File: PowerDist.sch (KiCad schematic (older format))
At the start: 12 parts, among them U4 RI3-1205S, U5 NCP1117-3.3_SOT223

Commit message: Fixing merge issues
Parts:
- U4: symbol utsvt-power-regulators:RI3-1205S -> Controls-LightingPCB-rescue:RI3-1205S-utsvt-power-regulators
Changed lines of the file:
@@
 	8750 3200 8550 3200
 $Comp
-L utsvt-power-regulators:RI3-1205S U4
+L Controls-LightingPCB-rescue:RI3-1205S-utsvt-power-regulators U4
 U 1 1 5C38C4FE
 P 4500 3200

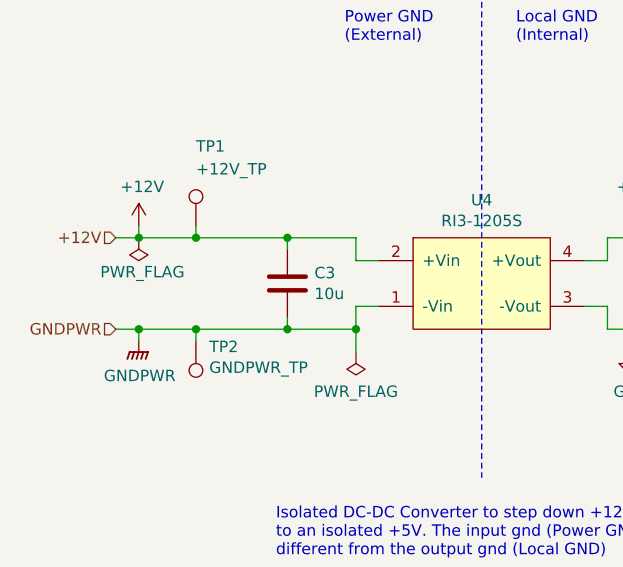
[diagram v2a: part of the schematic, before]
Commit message: Added resistor and diode
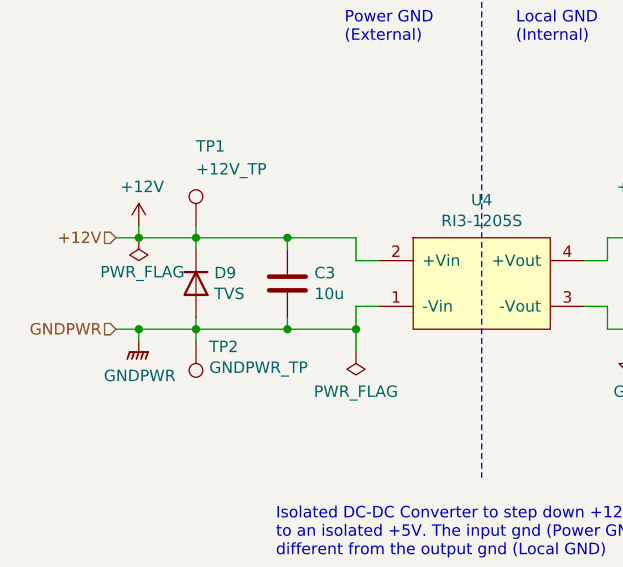
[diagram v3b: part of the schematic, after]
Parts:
- added D9: TVS, Diode_SMD:D_SOD-323, symbol Simulation_SPICE:DIODE
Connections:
- net +12V: now also D9.2 (K)
- net GNDPWR: now also D9.1 (A)
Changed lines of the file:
@@
 Wire Wire Line
 	2900 3600 3000 3600
+$Comp
+L Simulation_SPICE:DIODE D9
+U 1 1 615A7A80
+P 3250 3400
+F 0 "D9" V 3296 3320 50  0000 R CNN
+F 1 "TVS" V 3205 3320 50  0000 R CNN
+F 2 "Diode_SMD:D_SOD-323" H 3250 3400 50  0001 C CNN
+F 3 "~" H 3250 3400 50  0001 C CNN
+F 4 "Y" H 3250 3400 50  0001 L CNN "Spice_Netlist_Enabled"
+F 5 "D" H 3250 3400 50  0001 L CNN "Spice_Primitive"
+	1    3250 3400
+	0    -1   -1   0
+$EndComp
+Wire Wire Line
+	3250 3250 3250 3200
+Wire Wire Line
+	3250 3550 3250 3600
 $EndSCHEMATC

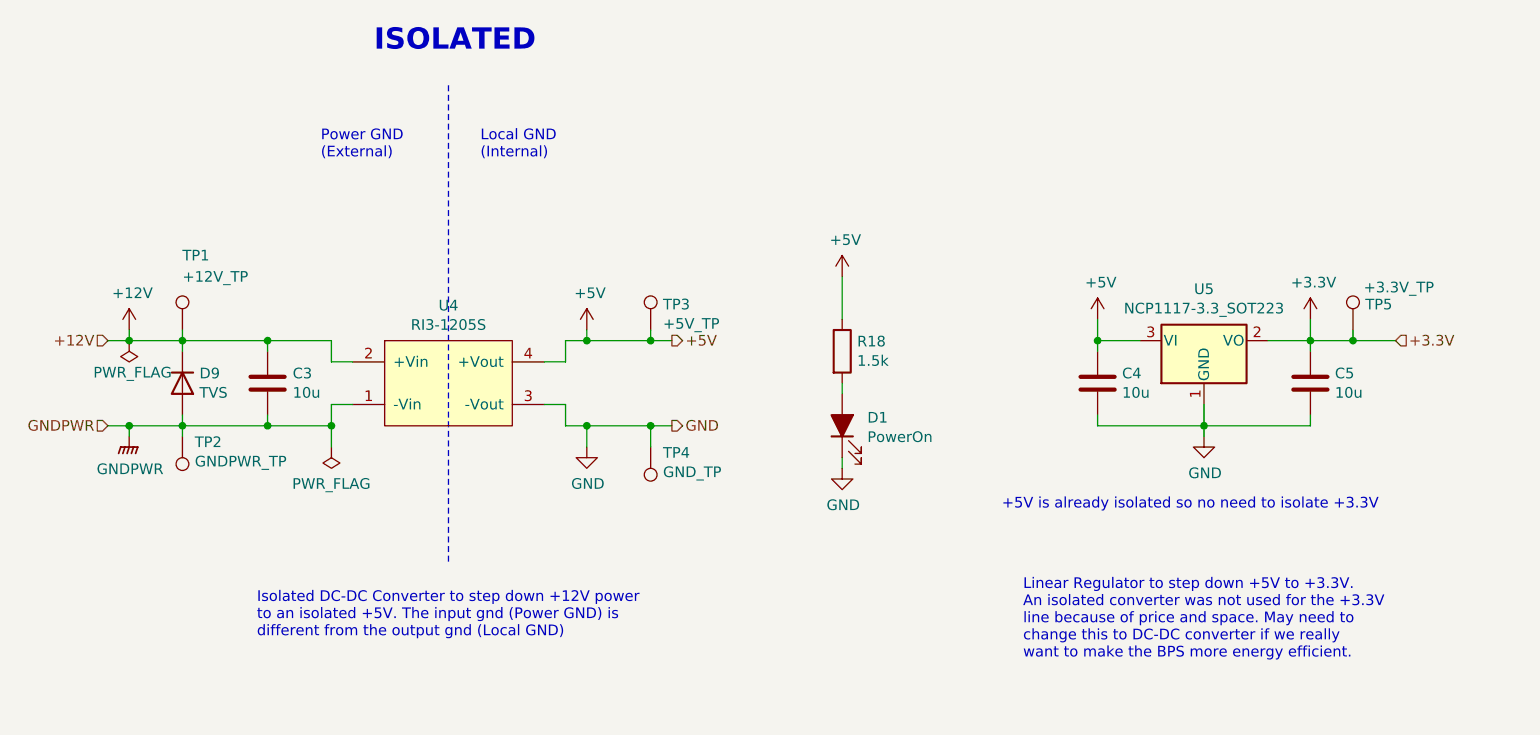
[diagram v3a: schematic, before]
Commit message: isoSPI -> SPI change
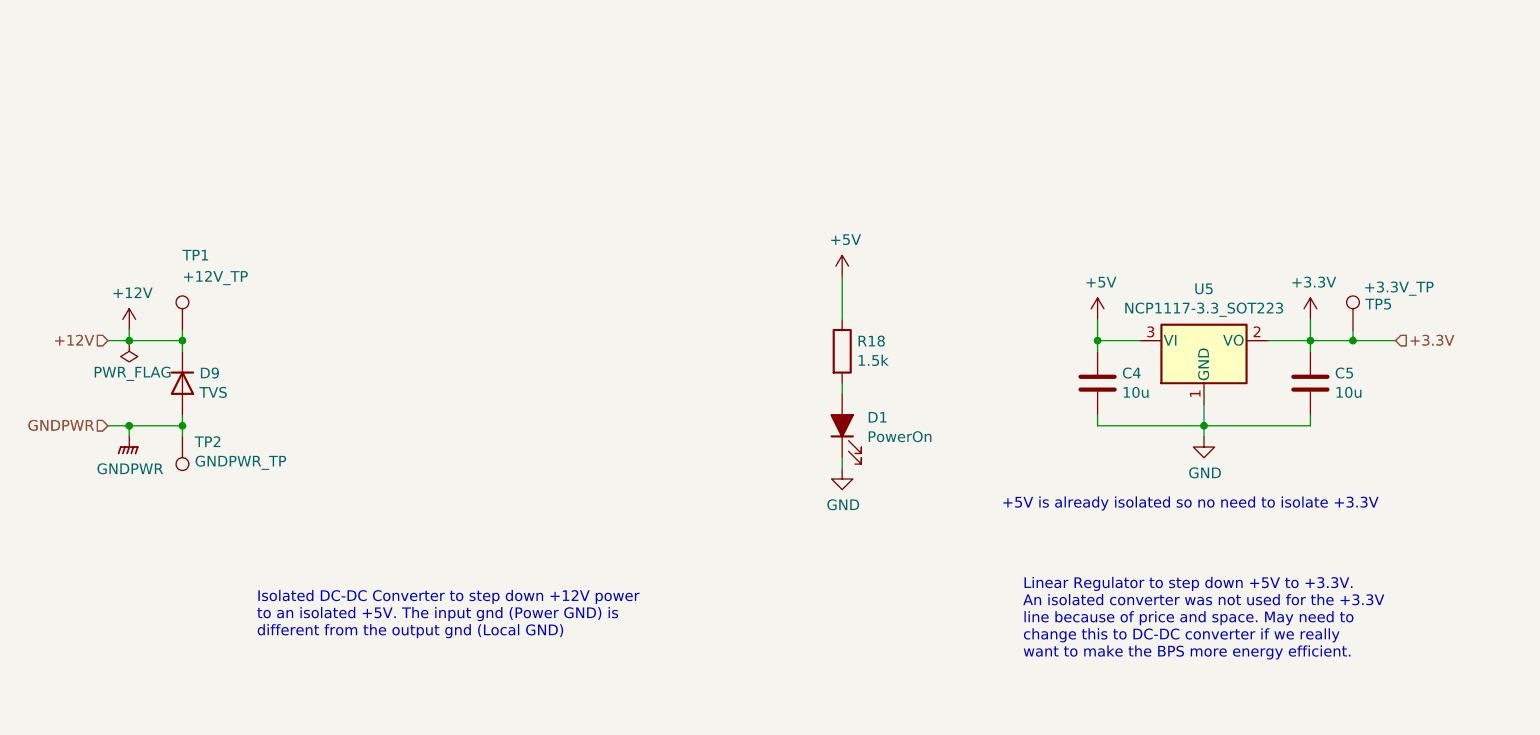
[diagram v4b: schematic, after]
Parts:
- removed C3: 10u, UTSVT_Passive:C_2220_5750Metric, symbol Device:C
- removed TP3: +5V_TP, TestPoint:TestPoint_Pad_1.5x1.5mm, symbol Connector:TestPoint
- removed TP4: GND_TP, TestPoint:TestPoint_Pad_1.5x1.5mm, symbol Connector:TestPoint
- removed U4: RI3-1205S, UTSVT_ICs:RI3_DC_Converter, symbol Controls-LightingPCB-rescue:RI3-1205S-utsvt-power-regulators
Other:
- note removed: "ISOLATED"
- note removed: "Local GND\n(Internal)"
- note removed: "Power GND\n(External)"
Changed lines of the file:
@@
 Wire Wire Line
 	3000 3600 3000 3650
-$Comp
-L Device:C C3
-U 1 1 5C35F7E4
-P 3650 3400
-F 0 "C3" H 3768 3446 50  0000 L CNN
-F 1 "10u" H 3768 3355 50  0000 L CNN
-F 2 "UTSVT_Passive:C_2220_5750Metric" H 3688 3250 50  0001 C CNN
-F 3 "~" H 3650 3400 50  0001 C CNN
-	1    3650 3400
-	1    0    0    -1
-$EndComp
 Wire Wire Line
 	3000 3600 3250 3600
@@
 	3000 3200 3250 3200
 Connection ~ 3000 3200
-Wire Wire Line
-	3650 3250 3650 3200
 Connection ~ 3250 3200
-Wire Wire Line
-	3650 3550 3650 3600
-Wire Wire Line
-	5150 3700 5150 3600
-Connection ~ 5150 3600
-Wire Wire Line
-	5450 3600 5150 3600
-Wire Wire Line
-	5150 3150 5150 3200
-Text HLabel 5550 3600 2    50   Output ~ 0
-GND
-Wire Wire Line
-	5550 3600 5450 3600
-Connection ~ 5450 3600
-Text HLabel 5550 3200 2    50   Output ~ 0
-+5V
-$Comp
-L power:+5V #PWR04
-U 1 1 5C376123
-P 5150 3150
-F 0 "#PWR04" H 5150 3000 50  0001 C CNN
-F 1 "+5V" H 5165 3323 50  0000 C CNN
-F 2 "" H 5150 3150 50  0001 C CNN
-F 3 "" H 5150 3150 50  0001 C CNN
-	1    5150 3150
-	1    0    0    -1
-$EndComp
 $Comp
 L Connector:TestPoint TP1
@@
 Wire Wire Line
 	3250 3150 3250 3200
-$Comp
-L Connector:TestPoint TP3
-U 1 1 5C37E6A3
-P 5450 3150
-F 0 "TP3" H 5508 3270 50  0000 L CNN
-F 1 "+5V_TP" H 5508 3179 50  0000 L CNN
-F 2 "TestPoint:TestPoint_Pad_1.5x1.5mm" H 5650 3150 50  0001 C CNN
-F 3 "~" H 5650 3150 50  0001 C CNN
-	1    5450 3150
-	1    0    0    -1
-$EndComp
-Wire Wire Line
-	5450 3150 5450 3200
-$Comp
-L Connector:TestPoint TP4
-U 1 1 5C37F6B1
-P 5450 3700
-F 0 "TP4" H 5392 3727 50  0000 R CNN
-F 1 "GND_TP" H 5392 3818 50  0000 R CNN
-F 2 "TestPoint:TestPoint_Pad_1.5x1.5mm" H 5650 3700 50  0001 C CNN
-F 3 "~" H 5650 3700 50  0001 C CNN
-	1    5450 3700
-	-1   0    0    1
-$EndComp
-Wire Wire Line
-	5450 3700 5450 3600
 $Comp
 L power:GND #PWR07
@@
 $EndComp
 $Comp
-L power:GND #PWR05
-U 1 1 5C3F3B1F
-P 5150 3700
-F 0 "#PWR05" H 5150 3450 50  0001 C CNN
-F 1 "GND" H 5155 3527 50  0000 C CNN
-F 2 "" H 5150 3700 50  0001 C CNN
-F 3 "" H 5150 3700 50  0001 C CNN
-	1    5150 3700
-	1    0    0    -1
-$EndComp
-$Comp
 L power:GNDPWR #PWR03
 U 1 1 5C3F7204
@@
 Wire Wire Line
 	8750 3200 8550 3200
-$Comp
-L Controls-LightingPCB-rescue:RI3-1205S-utsvt-power-regulators U4
-U 1 1 5C38C4FE
-P 4500 3200
-F 0 "U4" H 4500 3365 50  0000 C CNN
-F 1 "RI3-1205S" H 4500 3274 50  0000 C CNN
-F 2 "UTSVT_ICs:RI3_DC_Converter" H 4500 3200 50  0001 C CNN
-F 3 "" H 4500 3200 50  0001 C CNN
-	1    4500 3200
-	1    0    0    -1
-$EndComp
-Wire Wire Line
-	3950 3500 4050 3500
-Wire Wire Line
-	3950 3300 4050 3300
-Wire Wire Line
-	4950 3300 5050 3300
-Wire Wire Line
-	5050 3300 5050 3200
-Wire Wire Line
-	4950 3500 5050 3500
-Wire Wire Line
-	5050 3500 5050 3600
-Wire Wire Line
-	5050 3600 5150 3600
-Wire Wire Line
-	5050 3200 5150 3200
-Connection ~ 5150 3200
-Wire Wire Line
-	5150 3200 5450 3200
-Connection ~ 5450 3200
-Wire Wire Line
-	5450 3200 5550 3200
 $Comp
 L Connector:TestPoint TP2
@@
 +5V is already isolated so no need to isolate +3.3V
 $Comp
-L power:PWR_FLAG #FLG02
-U 1 1 5F1EAFA2
-P 3950 3700
-F 0 "#FLG02" H 3950 3775 50  0001 C CNN
-F 1 "PWR_FLAG" H 3950 3873 50  0000 C CNN
-F 2 "" H 3950 3700 50  0001 C CNN
-F 3 "~" H 3950 3700 50  0001 C CNN
-	1    3950 3700
-	-1   0    0    1
-$EndComp
-$Comp
 L power:PWR_FLAG #FLG01
 U 1 1 5F1F32D3
@@
 Wire Wire Line
 	2900 3200 3000 3200
-Text Notes 4150 1850 0    100  ~ 20
-ISOLATED
-Text Notes 4650 2350 0    50   ~ 0
-Local GND\n(Internal)
-Text Notes 3900 2350 0    50   ~ 0
-Power GND\n(External)
 Text Notes 7200 4700 0    50   ~ 0
 Linear Regulator to step down +5V to +3.3V.\nAn isolated converter was not used for the +3.3V\nline because of price and space. May need to\nchange this to DC-DC converter if we really\nwant to make the BPS more energy efficient.
-Wire Notes Line
-	4500 2000 4500 4250
 Text Notes 3600 4600 0    50   ~ 0
 Isolated DC-DC Converter to step down +12V power\nto an isolated +5V. The input gnd (Power GND) is\ndifferent from the output gnd (Local GND)
-Wire Wire Line
-	3250 3200 3650 3200
-Connection ~ 3650 3200
-Wire Wire Line
-	3650 3200 3950 3200
-Wire Wire Line
-	3250 3600 3650 3600
 Connection ~ 3250 3600
-Connection ~ 3650 3600
-Wire Wire Line
-	3650 3600 3950 3600
-Wire Wire Line
-	3950 3200 3950 3300
-Connection ~ 3950 3600
-Wire Wire Line
-	3950 3600 3950 3700
-Wire Wire Line
-	3950 3500 3950 3600
 Wire Wire Line
 	6350 2900 6350 3100

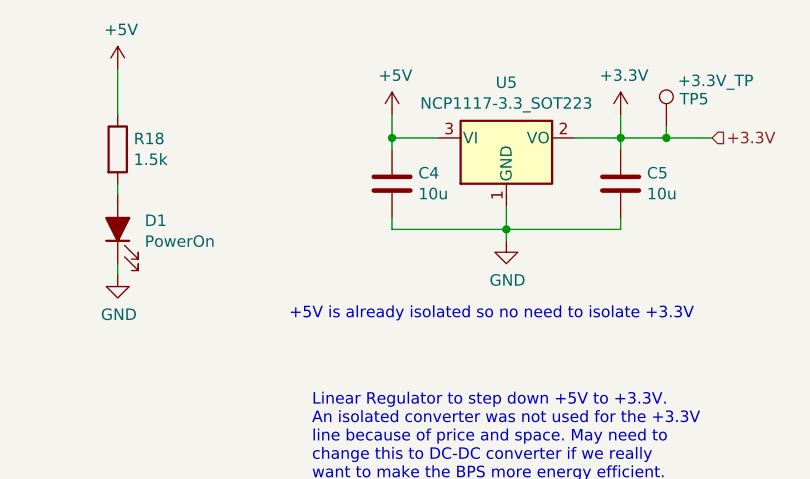
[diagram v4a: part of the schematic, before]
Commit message: isoSPI -> SPI 2
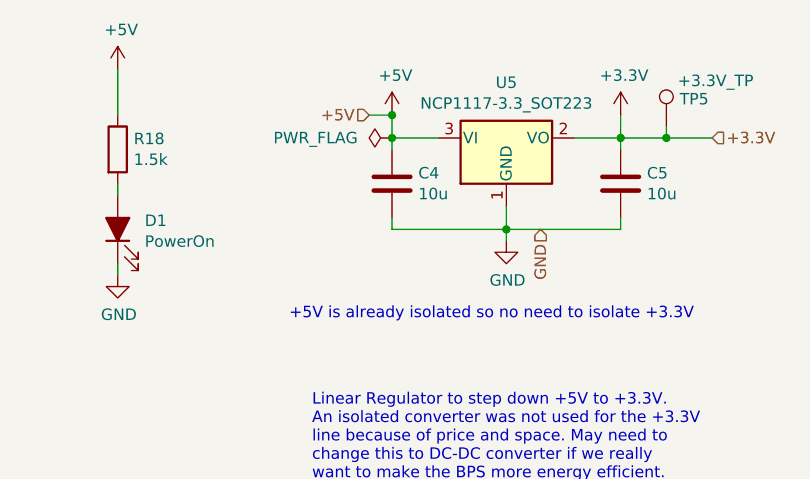
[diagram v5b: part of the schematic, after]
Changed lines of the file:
@@
 Wire Wire Line
 	3250 3550 3250 3600
+$Comp
+L power:PWR_FLAG #FLG0101
+U 1 1 61A11CC9
+P 7550 3200
+F 0 "#FLG0101" H 7550 3275 50  0001 C CNN
+F 1 "PWR_FLAG" V 7550 3350 50  0000 L CNN
+F 2 "" H 7550 3200 50  0001 C CNN
+F 3 "~" H 7550 3200 50  0001 C CNN
+	1    7550 3200
+	0    -1   -1   0
+$EndComp
+Wire Wire Line
+	7450 3100 7550 3100
+Connection ~ 7550 3100
+Text HLabel 7450 3100 0    50   Input ~ 0
++5V
+Text HLabel 8200 3600 3    50   Input ~ 0
+GND
 $EndSCHEMATC

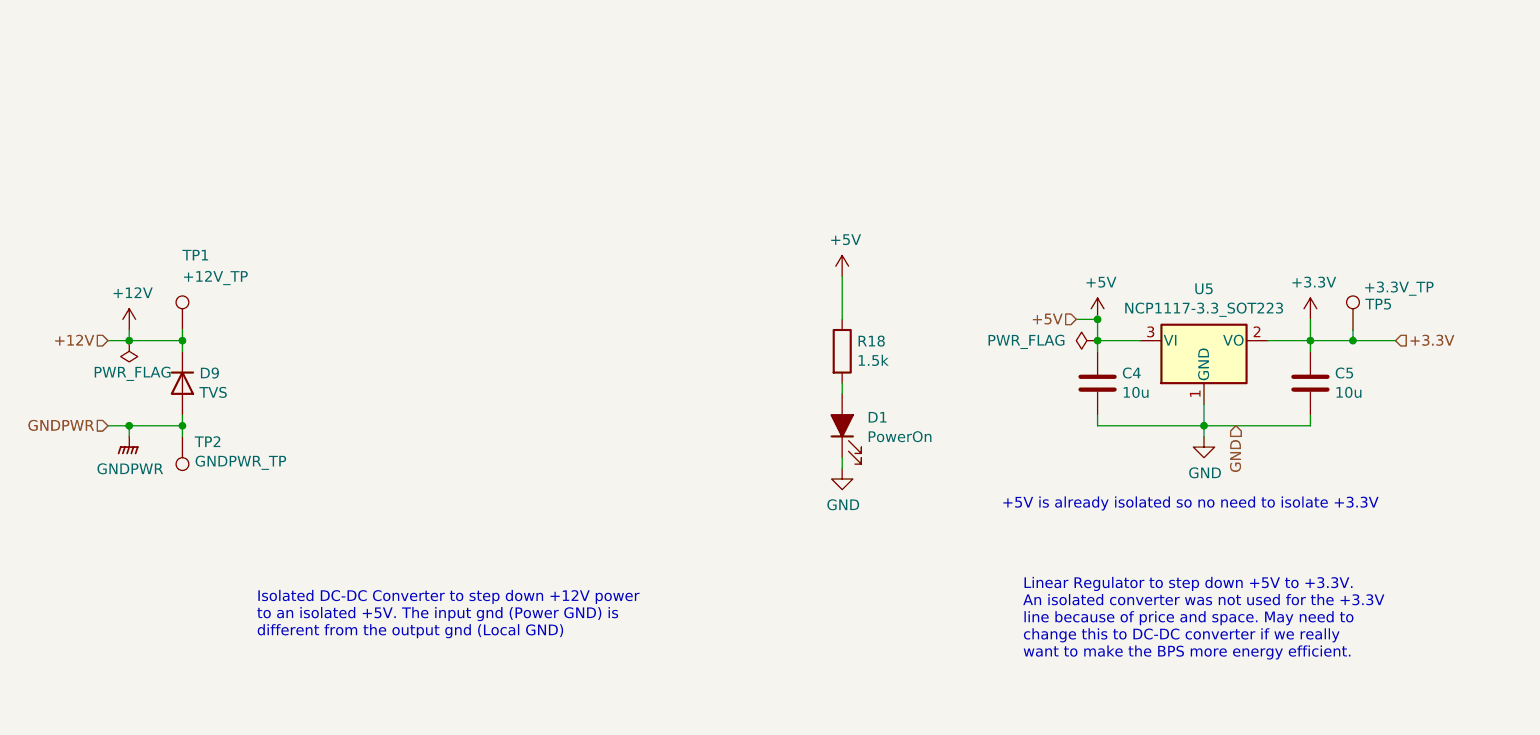
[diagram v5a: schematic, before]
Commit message: Deleted backup camera
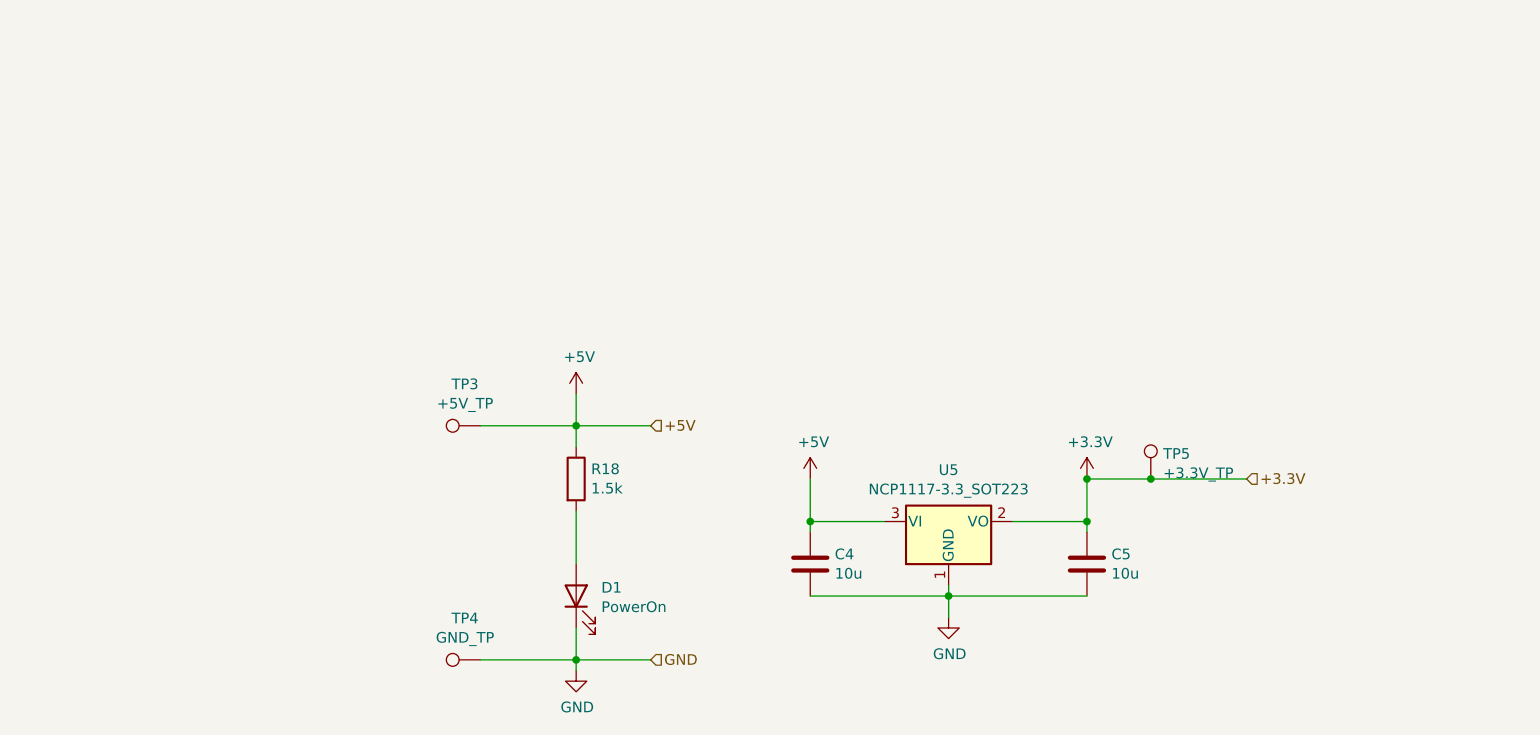
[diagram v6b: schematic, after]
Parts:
- removed D1: PowerOn, LED_SMD:LED_0805_2012Metric, symbol Device:LED_ALT
- removed D9: TVS, Diode_SMD:D_SOD-323, symbol Simulation_SPICE:DIODE
- removed TP1: +12V_TP, TestPoint:TestPoint_Pad_1.5x1.5mm, symbol Connector:TestPoint
- removed TP2: GNDPWR_TP, TestPoint:TestPoint_Pad_1.5x1.5mm, symbol Connector:TestPoint
- removed U5: NCP1117-3.3_SOT223, Package_TO_SOT_SMD:SOT-223-3_TabPin2, symbol Regulator_Linear:LD1117S33TR_SOT223
- added D1: PowerOn, LED_SMD:LED_0805_2012Metric, symbol Device:LED
- added TP3: +5V_TP, TestPoint:TestPoint_Pad_1.5x1.5mm, symbol Connector:TestPoint
- added TP4: GND_TP, TestPoint:TestPoint_Pad_1.5x1.5mm, symbol Connector:TestPoint
- added U5: NCP1117-3.3_SOT223, Package_TO_SOT_SMD:SOT-223-3_TabPin2, symbol Regulator_Linear:NCP1117-3.3_SOT223
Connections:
- net +3V3: now also U5.2 (VO)
- net +5V: now also TP3.1, U5.3 (VI)
- net GND: now also D1.1 (K), TP4.1, U5.1 (GND)
- net at R18.2: now also D1.2 (A)
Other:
- note removed: "+5V is already isolated so no need to isolate +3.3V"
- note removed: "Isolated DC-DC Converter to step down +12V power\nto an isolated +5V. The input gnd (Power GND) is\ndifferent from the output gnd (Local GND)"
- note removed: "Linear Regulator to step down +5V to +3.3V.\nAn isolated converter was not used for the +3.3V\nline because of price and space. May need to\nchange this to DC-DC converter if we really\nwant to make the BPS more energy efficient."
